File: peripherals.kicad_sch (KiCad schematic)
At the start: 46 parts, among them J12 PinHeader_2x5_P1.27mm_SMD, J13 PinHeader_2x5_P1.27mm_SMD, J14 PinHeader_2x5_P1.27mm_SMD, J15 PinHeader_2x5_P1.27mm_SMD, J16 PinHeader_2x5_P1.27mm_SMD, J20 PinHeader_2x5_P1.27mm_SMD, J6 PinHeader_2x10_P1.27mm_SMD_Sh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, J7 JST_SH_1x4_BM04B-SRSS-TB-LF-SN, J8 PinHeader_1x2_P1.27mm_Drill0.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, J9 PinHeader_2x5_P1.27mm_SMD_Shr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, Q2 DMG1012T-7, Q3 DMG1012T-7, Q4 DMG1012T-7, U1 TMP75AIDR, U2 AT24C04C_SOIC8

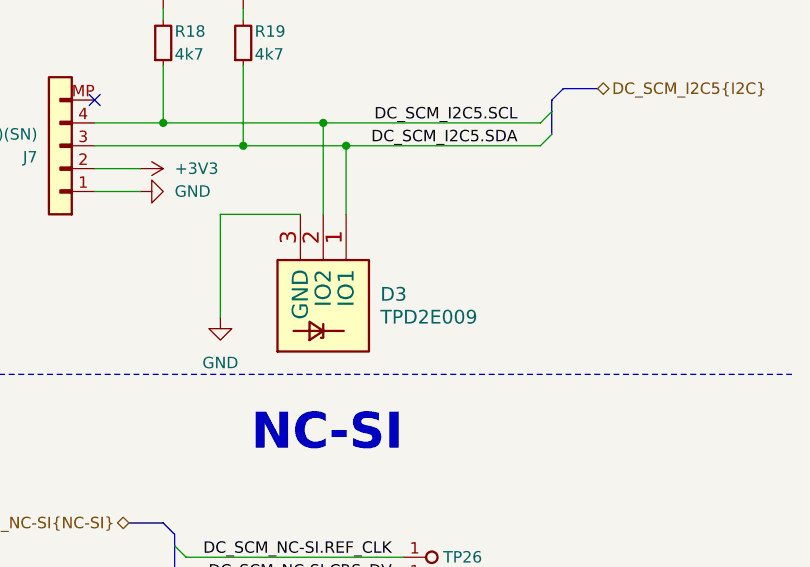
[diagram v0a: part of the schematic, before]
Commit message: [#93949] Replace TVS diodes, remove references to project library component
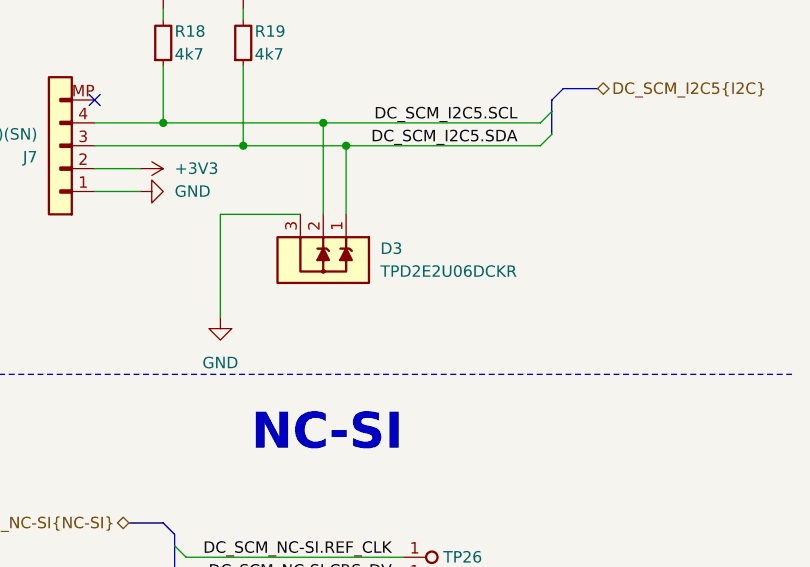
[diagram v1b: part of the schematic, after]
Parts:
- removed D3: TPD2E009, bmc-breakout-board-footprints:SOT-3, symbol bmc-breakout-board:TPD2E009
- added D3: TPD2E2U06_SC70, antmicro-footprints:SC70-3, symbol antmicroTVSDiodes:TPD2E2U06_SC70
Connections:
- net DC_SCM_I2C5.SCL: now also D3.2
- net DC_SCM_I2C5.SDA: now also D3.1
- net GND: now also D3.3
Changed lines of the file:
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@@
 	)
 	(symbol
-		(lib_id "bmc-breakout-board:TPD2E009")
-		(at 358.14 60.96 270)
-		(unit 1)
-		(exclude_from_sim no)
-		(in_bom yes)
-		(on_board yes)
-		(dnp no)
-		(fields_autoplaced yes)
-		(property "Reference" "D3"
-			(at 361.95 64.7699 90)
-			(effects
-				(font
-					(size 1.524 1.524)
-				)
-				(justify left)
-			)
-		)
-		(property "Value" "TPD2E009"
-			(at 361.95 67.3099 90)
-			(effects
-				(font
-					(size 1.524 1.524)
-				)
-				(justify left)
-			)
-		)
-		(property "Footprint" "bmc-breakout-board-footprints:SOT-3"
-			(at 363.22 62.23 0)
-			(effects
-				(font
-					(size 1.524 1.524)
-				)
-				(hide yes)
-			)
-		)
-		(property "Datasheet" ""
-			(at 358.14 60.96 0)
-			(effects
-				(font
-					(size 1.524 1.524)
-				)
-				(hide yes)
-			)
-		)
-		(property "Description" ""
-			(at 358.14 60.96 0)
-			(effects
-				(font
-					(size 1.27 1.27)
-				)
-				(hide yes)
-			)
-		)
-		(property "MPN" "TPD2E009DRTR"
-			(at 365.76 53.34 0)
-			(effects
-				(font
-					(size 1.27 1.27)
-				)
-				(hide yes)
-			)
-		)
-		(property "Manufacturer" "Texas Instruments"
-			(at 368.3 53.34 0)
-			(effects
-				(font
-					(size 1.27 1.27)
-				)
-				(hide yes)
-			)
-		)
-		(pin "3"
-		)
-		(pin "2"
-		)
-		(pin "1"
-		)
-		(instances
-			(project "bmc-breakout-board"
-				(path "/5d67ef28-5805-4f87-b722-2926dabf7f6e/f1ecdd24-c7ef-4765-8186-53d06f23944d"
-					(reference "D3")
-					(unit 1)
-				)
-			)
-		)
-	)
-	(symbol
 		(lib_id "antmicroResistors0402:R_4k7_0402")
 		(at 337.82 39.37 90)
@@
 					(unit 1)
 				)
+			)
+		)
+	)
+	(symbol
+		(lib_id "antmicroTVSDiodes:TPD2E2U06_SC70")
+		(at 358.14 55.88 270)
+		(unit 1)
+		(exclude_from_sim no)
+		(in_bom yes)
+		(on_board yes)
+		(dnp no)
+		(fields_autoplaced yes)
+		(property "Reference" "D3"
+			(at 361.95 59.69 90)
+			(effects
+				(font
+					(size 1.27 1.27)
+					(thickness 0.15)
+				)
+				(justify left)
+			)
+		)
+		(property "Value" "TPD2E2U06_SC70"
+			(at 355.6 68.58 0)
+			(effects
+				(font
+					(size 1.27 1.27)
+					(thickness 0.15)
+				)
+				(justify left bottom)
+				(hide yes)
+			)
+		)
+		(property "Footprint" "antmicro-footprints:SC70-3"
+			(at 353.06 68.58 0)
+			(effects
+				(font
+					(size 1.27 1.27)
+					(thickness 0.15)
+				)
+				(justify left bottom)
+				(hide yes)
+			)
+		)
+		(property "Datasheet" "https://www.ti.com/lit/ds/symlink/tpd2e2u06.pdf?ts=1706006131823&ref_url=https%253A%252F%252Fwww.ti.com%252Finterface%252Fdiodes%252Fesd-protection-diodes%252Fproducts.html"
+			(at 350.52 68.58 0)
+			(effects
+				(font
+					(size 1.27 1.27)
+					(thickness 0.15)
+				)
+				(justify left bottom)
+				(hide yes)
+			)
+		)
+		(property "Description" "TVS diode array, 15 kV, SC70, 5.5V, 1.5 pF"
+			(at 340.36 68.58 0)
+			(effects
+				(font
+					(size 1.27 1.27)
+				)
+				(justify left bottom)
+				(hide yes)
+			)
+		)
+		(property "MPN" "TPD2E2U06DCKR"
+			(at 361.95 62.23 90)
+			(effects
+				(font
+					(size 1.27 1.27)
+					(thickness 0.15)
+				)
+				(justify left)
+			)
+		)
+		(property "Manufacturer" "Texas Instruments"
+			(at 347.98 68.58 0)
+			(effects
+				(font
+					(size 1.27 1.27)
+					(thickness 0.15)
+				)
+				(justify left bottom)
+				(hide yes)
+			)
+		)
+		(property "Author" "Antmicro"
+			(at 345.44 68.58 0)
+			(effects
+				(font
+					(size 1.27 1.27)
+					(thickness 0.15)
+				)
+				(justify left bottom)
+				(hide yes)
+			)
+		)
+		(property "License" "Apache-2.0"
+			(at 342.9 68.58 0)
+			(effects
+				(font
+					(size 1.27 1.27)
+					(thickness 0.15)
+				)
+				(justify left bottom)
+				(hide yes)
+			)
+		)
+		(pin "3"
+		)
+		(pin "2"
+		)
+		(pin "1"
+		)
+		(instances
+			(project "bmc-breakout-board"
+				(path "/5d67ef28-5805-4f87-b722-2926dabf7f6e/f1ecdd24-c7ef-4765-8186-53d06f23944d"
+					(reference "D3")
+					(unit 1)
+				)

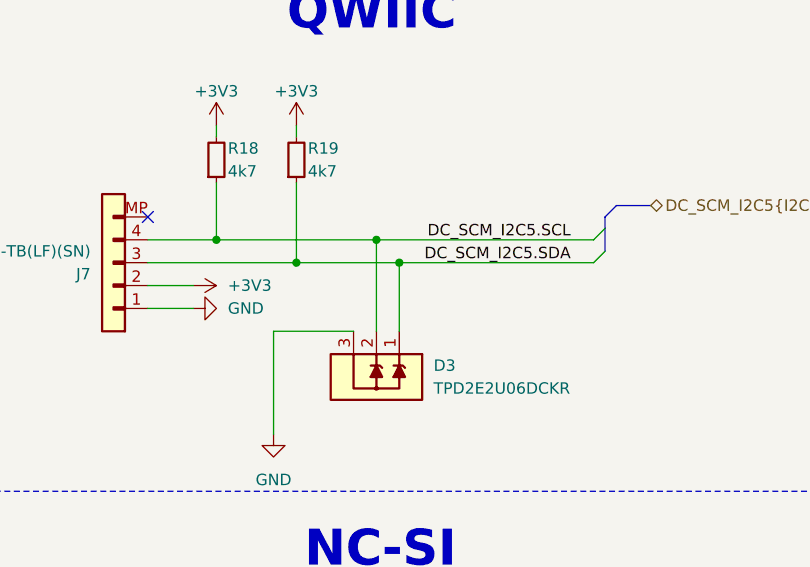
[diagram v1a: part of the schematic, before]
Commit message: [#94820] Move TVS all diodes except PCIE dioes to front layer
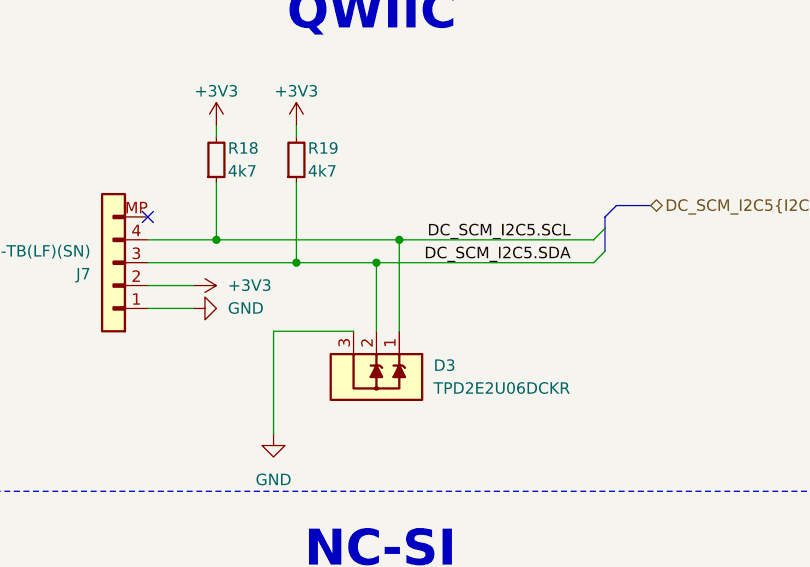
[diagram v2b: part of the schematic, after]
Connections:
- net DC_SCM_I2C5.SCL: now also D3.1; no longer D3.2
- net DC_SCM_I2C5.SDA: now also D3.2; no longer D3.1
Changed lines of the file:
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@@
 	)
 	(junction
-		(at 355.6 45.72)
+		(at 85.09 158.75)
 		(diameter 0)
 		(color 0 0 0 0)
 	)
 	(junction
-		(at 85.09 158.75)
+		(at 358.14 45.72)
+		(diameter 0)
+		(color 0 0 0 0)
+	)
+	(junction
+		(at 355.6 48.26)
 		(diameter 0)
 		(color 0 0 0 0)
@@
 	)
 	(junction
-		(at 358.14 48.26)
-		(diameter 0)
-		(color 0 0 0 0)
-	)
-	(junction
 		(at 63.5 227.33)
 		(diameter 0)
@@
 	(wire
 		(pts
-			(xy 337.82 45.72) (xy 355.6 45.72)
+			(xy 337.82 45.72) (xy 358.14 45.72)
 		)
 		(stroke
@@
 	(wire
 		(pts
+			(xy 358.14 55.88) (xy 358.14 45.72)
+		)
+		(stroke
+			(width 0)
+			(type default)
+		)
+	)
+	(wire
+		(pts
 			(xy 373.38 233.68) (xy 373.38 237.49)
 		)
@@
 		)
 	)
-	(wire
-		(pts
-			(xy 358.14 48.26) (xy 379.73 48.26)
-		)
-		(stroke
-			(width 0)
-			(type default)
-		)
-	)
 	(bus
 		(pts
@@
 	(wire
 		(pts
-			(xy 358.14 48.26) (xy 358.14 55.88)
-		)
-		(stroke
-			(width 0)
-			(type default)
-		)
-	)
-	(wire
-		(pts
 			(xy 260.35 264.16) (xy 260.35 261.62)
 		)
@@
 		)
 	)
+	(wire
+		(pts
+			(xy 358.14 45.72) (xy 379.73 45.72)
+		)
+		(stroke
+			(width 0)
+			(type default)
+		)
+	)
 	(bus
 		(pts
@@
 	(wire
 		(pts
-			(xy 355.6 45.72) (xy 379.73 45.72)
-		)
-		(stroke
-			(width 0)
-			(type default)
-		)
-	)
-	(wire
-		(pts
 			(xy 45.72 62.23) (xy 71.12 62.23)
 		)
@@
 		)
 	)
+	(wire
+		(pts
+			(xy 355.6 48.26) (xy 379.73 48.26)
+		)
+		(stroke
+			(width 0)
+			(type default)
+		)
+	)
 	(bus
 		(pts
@@
 	(wire
 		(pts
-			(xy 346.71 48.26) (xy 358.14 48.26)
+			(xy 346.71 48.26) (xy 355.6 48.26)
 		)
 		(stroke
@@
 		)
 	)
-	(wire
-		(pts
-			(xy 355.6 45.72) (xy 355.6 55.88)
-		)
-		(stroke
-			(width 0)
-			(type default)
-		)
-	)
 	(bus
 		(pts
@@
 		)
 		(stroke
+			(width 0)
+			(type default)
+		)
+	)
+	(wire
+		(pts
+			(xy 355.6 48.26) (xy 355.6 55.88)
+		)
+		(stroke
